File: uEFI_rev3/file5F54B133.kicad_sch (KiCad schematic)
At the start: 78 parts, among them Q14 AO3400A, Q15 AO3400A, Q16 AO3400A, U12 OPA340NA, U2 74HC4851, U27 LM321, U31 LM321, U9 OPA340NA

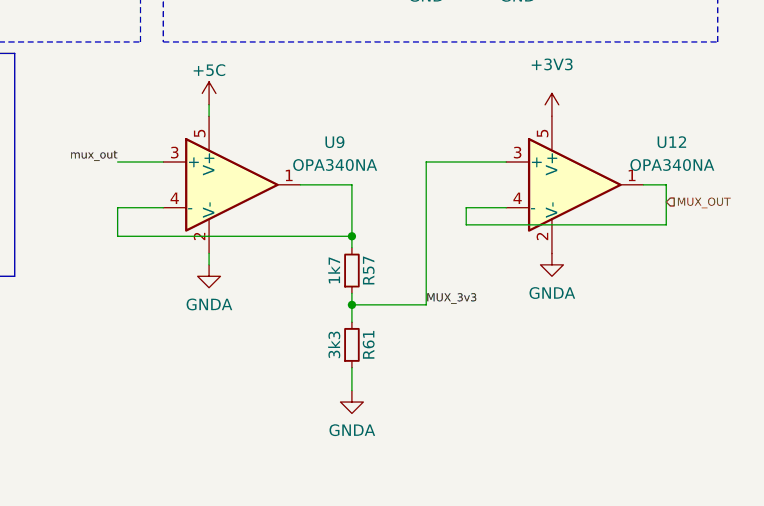
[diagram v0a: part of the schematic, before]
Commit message: fix bom output
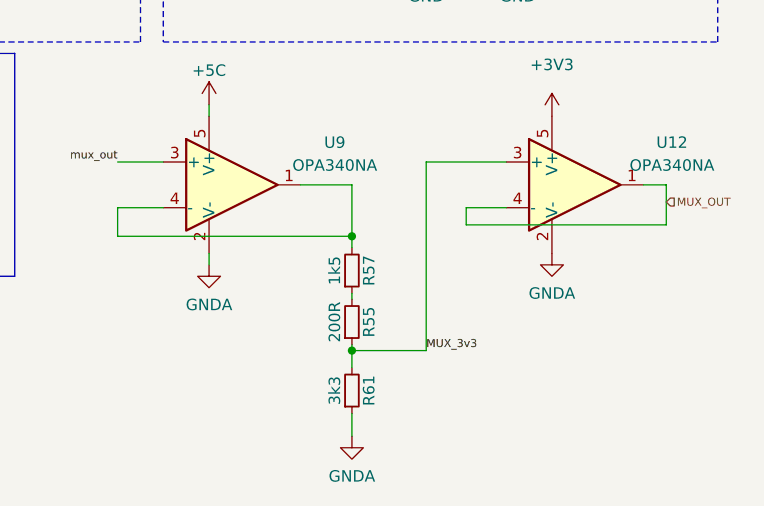
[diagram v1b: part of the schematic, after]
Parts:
- added R55: 200R, Resistor_SMD:R_0603_1608Metric, symbol Device:R_Small
- R57: value 1k7 -> 1k5
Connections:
- net MUX_3v3: now also R55.1; no longer R57.1
- new net: R55.2, R57.1
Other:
- moved on the sheet: R61
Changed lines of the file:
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@@
   (junction (at 124.46 90.805) (diameter 0) (color 0 0 0 0)
   )
+  (junction (at 266.7 191.77) (diameter 0) (color 0 0 0 0)
+  )
   (junction (at 210.82 133.985) (diameter 1.016) (color 0 0 0 0)
   )
@@
   (junction (at 151.13 90.805) (diameter 0) (color 0 0 0 0)
   )
-  (junction (at 266.7 186.69) (diameter 0) (color 0 0 0 0)
-  )
   (junction (at 165.1 90.805) (diameter 0) (color 0 0 0 0)
   )
@@
     (stroke (width 0) (type default) (color 0 0 0 0))
   )
+  (wire (pts (xy 266.7 185.42) (xy 266.7 186.055))
+    (stroke (width 0) (type default) (color 0 0 0 0))
+  )
   (wire (pts (xy 205.74 125.095) (xy 201.93 125.095))
     (stroke (width 0) (type solid) (color 0 0 0 0))
   )
+  (wire (pts (xy 266.7 191.77) (xy 266.7 193.675))
+    (stroke (width 0) (type default) (color 0 0 0 0))
+  )
   (polyline (pts (xy 179.07 114.3) (xy 140.335 114.3))
     (stroke (width 0) (type default) (color 0 0 0 0))
@@
     (stroke (width 0) (type default) (color 0 0 0 0))
   )
+  (wire (pts (xy 266.7 191.135) (xy 266.7 191.77))
+    (stroke (width 0) (type default) (color 0 0 0 0))
+  )
   (wire (pts (xy 124.46 93.345) (xy 124.46 90.805))
     (stroke (width 0) (type default) (color 0 0 0 0))
@@
     (stroke (width 0) (type default) (color 0 0 0 0))
   )
-  (wire (pts (xy 266.7 185.42) (xy 266.7 186.69))
-    (stroke (width 0) (type default) (color 0 0 0 0))
-  )
   (wire (pts (xy 120.015 168.275) (xy 121.92 168.275))
     (stroke (width 0) (type default) (color 0 0 0 0))
@@
     (stroke (width 0) (type default) (color 0 0 0 0))
   )
-  (wire (pts (xy 274.955 186.69) (xy 274.955 170.815))
+  (wire (pts (xy 274.955 191.77) (xy 274.955 170.815))
     (stroke (width 0) (type default) (color 0 0 0 0))
   )
@@
     (stroke (width 0) (type default) (color 0 0 0 0))
   )
-  (wire (pts (xy 266.7 186.69) (xy 266.7 188.595))
-    (stroke (width 0) (type default) (color 0 0 0 0))
-  )
   (wire (pts (xy 229.87 122.555) (xy 231.775 122.555))
     (stroke (width 0) (type default) (color 0 0 0 0))
@@
     (stroke (width 0) (type default) (color 0 0 0 0))
   )
-  (wire (pts (xy 266.7 193.675) (xy 266.7 196.215))
+  (wire (pts (xy 266.7 198.755) (xy 266.7 201.295))
     (stroke (width 0) (type default) (color 0 0 0 0))
   )
@@
     (stroke (width 0) (type default) (color 0 0 0 0))
   )
-  (wire (pts (xy 266.7 186.69) (xy 274.955 186.69))
+  (wire (pts (xy 266.7 191.77) (xy 274.955 191.77))
     (stroke (width 0) (type default) (color 0 0 0 0))
   )
@@
     (effects (font (size 0.889 0.889)) (justify left bottom))
   )
-  (label "MUX_3v3" (at 274.955 186.69 0)
+  (label "MUX_3v3" (at 274.955 191.77 0)
     (effects (font (size 0.889 0.889)) (justify left bottom))
   )
@@
     (pin "2")
   )
-  (symbol (lib_id "Device:R_Small") (at 266.7 191.135 0) (mirror x) (unit 1)
+  (symbol (lib_id "Device:R_Small") (at 266.7 196.215 0) (mirror x) (unit 1)
     (in_bom yes) (on_board yes)
-    (property "Reference" "R61" (id 0) (at 268.605 191.135 90))
-    (property "Value" "3k3" (id 1) (at 264.795 191.135 90))
-    (property "Footprint" "Resistor_SMD:R_0603_1608Metric" (id 2) (at 266.7 191.135 0)
+    (property "Reference" "R61" (id 0) (at 268.605 196.215 90))
+    (property "Value" "3k3" (id 1) (at 264.795 196.215 90))
+    (property "Footprint" "Resistor_SMD:R_0603_1608Metric" (id 2) (at 266.7 196.215 0)
       (effects (font (size 1.27 1.27)) hide)
     )
-    (property "Datasheet" "~" (id 3) (at 266.7 191.135 0)
+    (property "Datasheet" "~" (id 3) (at 266.7 196.215 0)
       (effects (font (size 1.27 1.27)) hide)
     )
@@
     (in_bom yes) (on_board yes)
     (property "Reference" "R57" (id 0) (at 268.605 182.88 90))
-    (property "Value" "1k7" (id 1) (at 264.795 182.88 90))
+    (property "Value" "1k5" (id 1) (at 264.795 182.88 90))
     (property "Footprint" "Resistor_SMD:R_0603_1608Metric" (id 2) (at 266.7 182.88 0)
       (effects (font (size 1.27 1.27)) hide)
@@
     (pin "1")
   )
+  (symbol (lib_id "Device:R_Small") (at 266.7 188.595 0) (mirror x) (unit 1)
+    (in_bom yes) (on_board yes)
+    (property "Reference" "R55" (id 0) (at 268.605 188.595 90))
+    (property "Value" "200R" (id 1) (at 264.795 188.595 90))
+    (property "Footprint" "Resistor_SMD:R_0603_1608Metric" (id 2) (at 266.7 188.595 0)
+      (effects (font (size 1.27 1.27)) hide)
+    )
+    (property "Datasheet" "~" (id 3) (at 266.7 188.595 0)
+      (effects (font (size 1.27 1.27)) hide)
+    )
+    (pin "1")
+    (pin "2")
+  )
   (symbol (lib_id "Device:R_Small") (at 151.13 128.905 180) (unit 1)
     (in_bom yes) (on_board yes)
@@
     (pin "2")
   )
-  (symbol (lib_id "power:GNDA") (at 266.7 196.215 0) (unit 1)
+  (symbol (lib_id "power:GNDA") (at 266.7 201.295 0) (unit 1)
     (in_bom yes) (on_board yes) (fields_autoplaced)
-    (property "Reference" "#PWR0138" (id 0) (at 266.7 202.565 0)
+    (property "Reference" "#PWR0138" (id 0) (at 266.7 207.645 0)
       (effects (font (size 1.27 1.27)) hide)
     )
-    (property "Value" "GNDA" (id 1) (at 266.7 200.66 0))
-    (property "Footprint" "" (id 2) (at 266.7 196.215 0)
+    (property "Value" "GNDA" (id 1) (at 266.7 205.74 0))
+    (property "Footprint" "" (id 2) (at 266.7 201.295 0)
       (effects (font (size 1.27 1.27)) hide)
     )
-    (property "Datasheet" "" (id 3) (at 266.7 196.215 0)
+    (property "Datasheet" "" (id 3) (at 266.7 201.295 0)
       (effects (font (size 1.27 1.27)) hide)
     )

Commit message: uEFI v3, fix 12v => 5v overcurrent issue
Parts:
- added R62, R63: 470R, Resistor_SMD:R_0603_1608Metric, symbol Device:R_Small
- added TP16: TestPoint, TestPoint:TestPoint_Pad_2.0x2.0mm, symbol Connector:TestPoint
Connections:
- net CH6: now also R62.1; no longer TP18.1, U31.3 (-), U31.4
- net CH7: now also R63.1; no longer TP19.1, U27.3 (-), U27.4
- net MUX_OUT: now also TP16.1
- new net: R62.2, TP18.1, U31.3 (-), U31.4
- new net: R63.2, TP19.1, U27.3 (-), U27.4
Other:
- moved on the sheet: D17, D20, D25, D28
